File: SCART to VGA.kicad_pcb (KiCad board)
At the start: 2 copper layers, 44.4 x 63.5 mm, 14 parts, among them J1 SCART-F, J2 Conn_01x03_Male, J3 USB_B_Micro, J4 DB15_Female_HighDensity, J5 AudioJack3, U1 LM1881

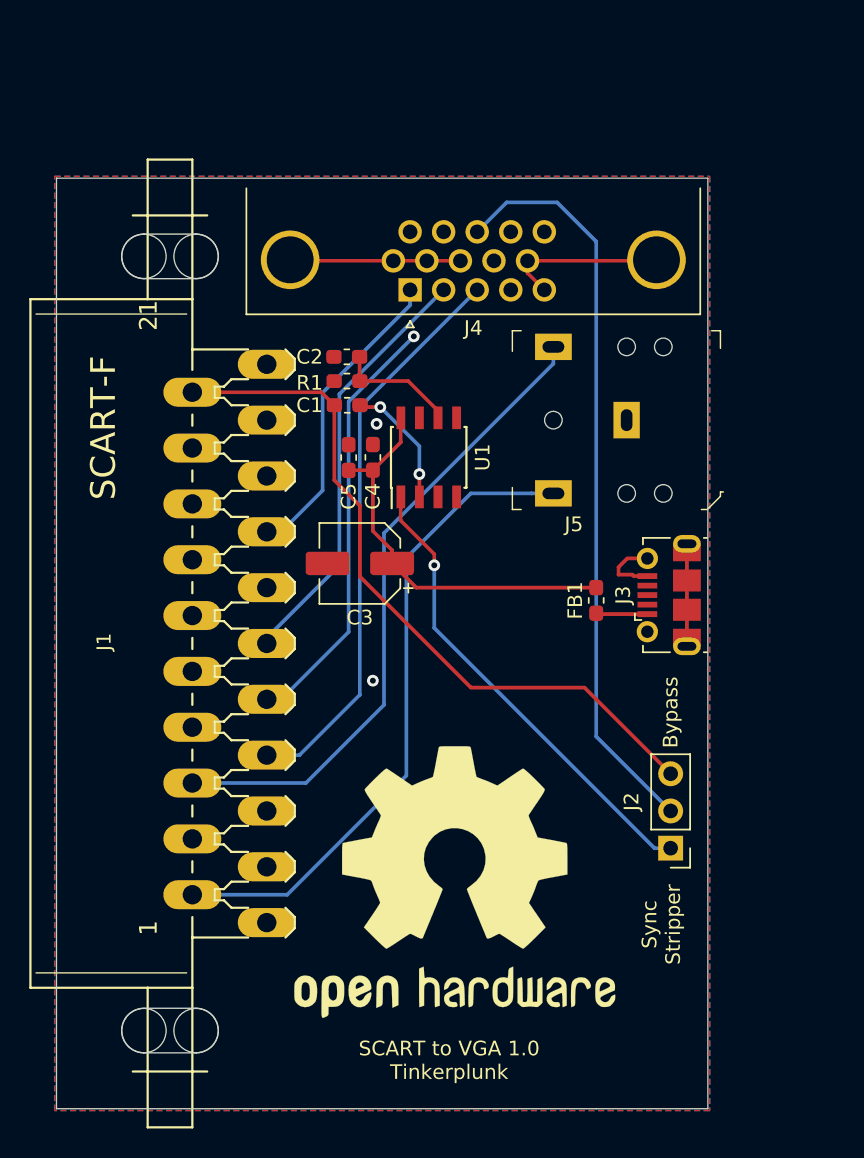
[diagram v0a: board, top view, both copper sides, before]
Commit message: Created branch
Branch where the SCART head lays on top of the PCB for direct plug in with a male hd-15 port.
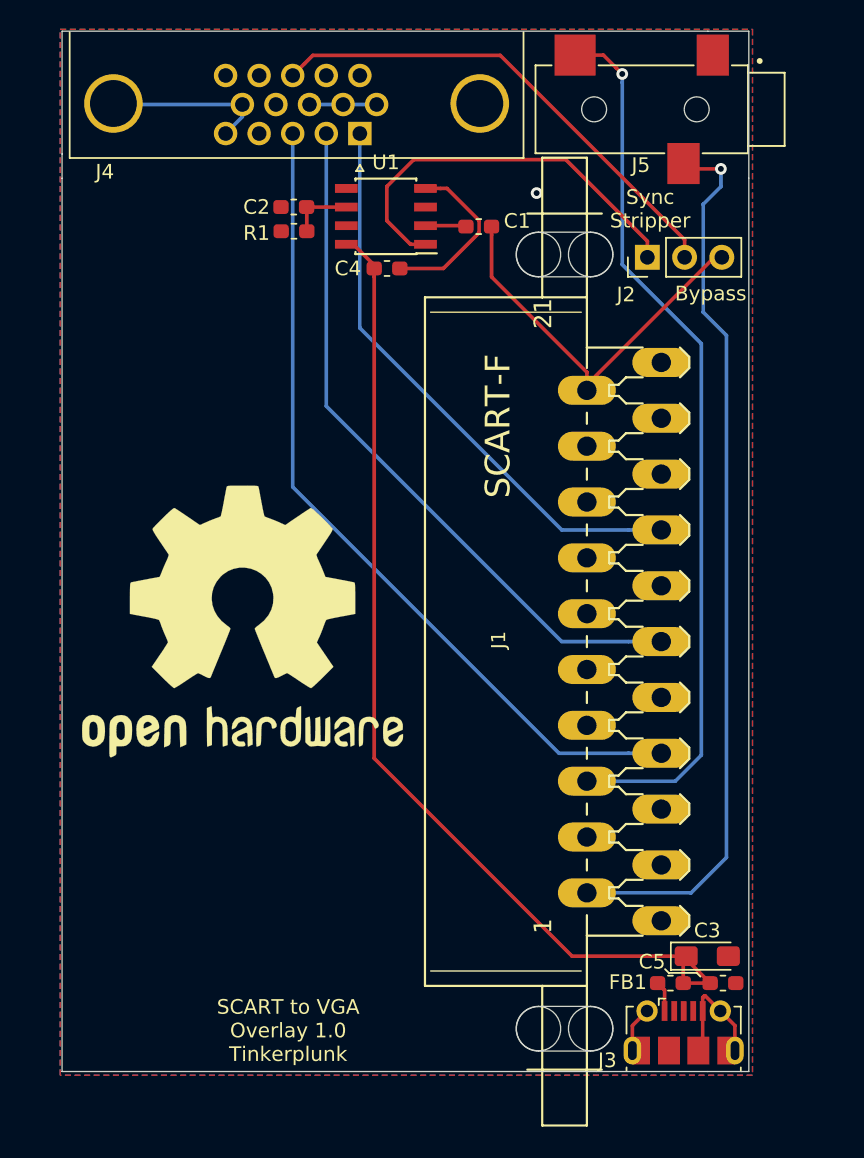
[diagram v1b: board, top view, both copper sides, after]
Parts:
- C3: footprint Capacitor_SMD:CP_Elec_5x5.3 -> Capacitor_Tantalum_SMD:CP_EIA-3216-18_Kemet-A_Pad1.58x1.35mm_HandSolder
- J4: footprint Connector_Dsub:DSUB-15-HD_Female_Horizontal_P2.29x1.98mm_EdgePinOffset3.03mm_Housed_MountingHolesOffset4.94mm -> Connector_Dsub:DSUB-15-HD_Male_Horizontal_P2.29x1.98mm_EdgePinOffset3.03mm_Housed_MountingHolesOffset4.94mm
- J5: footprint digikey-footprints:Headphone_Jack_3.5mm_SJ1-3523N -> SJ-3523-SMT-TR:CUI_SJ-3523-SMT-TR
- moved C5 44.0 mm to (120.4, 131.1), turned to 180 degrees
- moved J2 40.4 mm to (115.3, 81.6), turned to 90 degrees
- moved C3 35.8 mm to (119.3, 129.3), turned to 0 degrees
- moved J3 29.9 mm to (117.7, 134.5), turned to 0 degrees
- moved J1 26.9 mm to (111.1, 107.8)
- moved FB1 26.6 mm to (116.8, 131.1), turned to 0 degrees
- moved J5 23.4 mm to (118.6, 71.5)
- moved REF** 22.9 mm to (87.6, 106.4)
- moved U1 16.7 mm to (97.4, 78.8), turned to 180 degrees
- moved J4 16.6 mm to (91.1, 67.8)
- moved C1 15.1 mm to (103.7, 79.5), turned to 0 degrees
- moved C4 12.9 mm to (97.5, 82.4), turned to 180 degrees
- moved C2 10.8 mm to (91.1, 78.2)
- moved R1 10.8 mm to (91.1, 79.8)
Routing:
- net Net-(C3-Pad1): track 27.5 -> 69.3 mm
- net GND: track 63.6 -> 39.3 mm, vias 3 -> 1
- net SYNC_IN: track 49.2 -> 27.1 mm
- net GREEN: track 29.1 -> 48.1 mm
- net RED: track 21.1 -> 39.6 mm
- net BLUE: track 39.0 -> 56.8 mm
- net SYNC_OUT: track 51.0 -> 33.7 mm
- net RIGHT: track 44.7 -> 61.4 mm, vias 0 -> 1
- net LEFT: track 44.5 -> 61.0 mm, vias 0 -> 1
- net Net-(C1-Pad1): track 8.67 -> 2.79 mm, vias 2 -> 0
- net Net-(J2-Pad1): track 32.2 -> 27.6 mm, vias 1 -> 0
- net Net-(C2-Pad1): track 8.31 -> 4.37 mm
- net Net-(FB1-Pad1): track 3.51 -> 2.10 mm
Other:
- board size 44.4 x 63.5 mm -> 46.9 x 71 mm
- board text added: "SCART to VGA Overlay 1.0 Tinkerplunk"
- board text removed: "SCART to VGA 1.0 Tinkerplunk"

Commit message: 1.1 Update
Moved things around, made cutout for headphone jack, changed headphone jack part, added jumper for getting voltage optionally from the SCART socket.
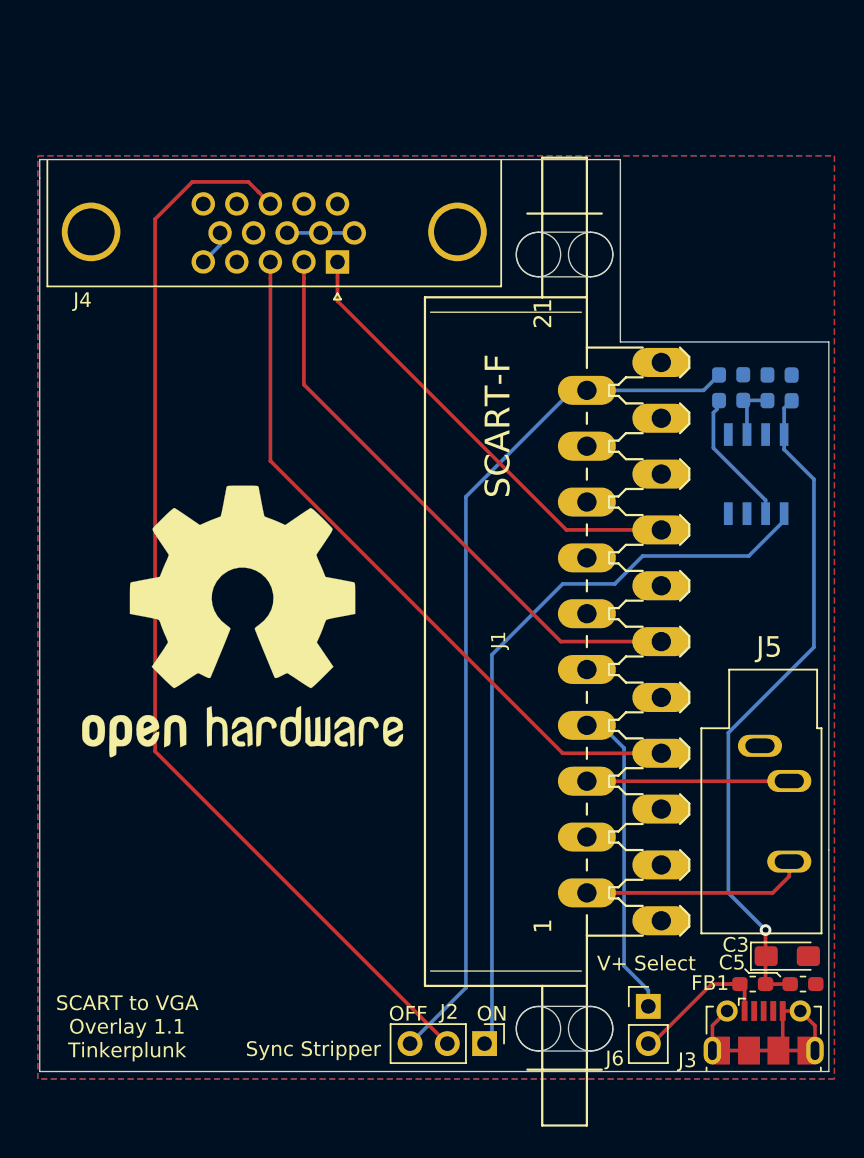
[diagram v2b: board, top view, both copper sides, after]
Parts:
- added J6: V+ Select, Connector_PinHeader_2.54mm:PinHeader_1x02_P2.54mm_Vertical, F.Cu at (115.3, 132.7)
- C1, C2, C4, R1, U1: moved to B.Cu
- J5: footprint SJ-3523-SMT-TR:CUI_SJ-3523-SMT-TR -> SJ1-3533NG:CUI_SJ1-3533NG
- moved J2 54.8 mm to (104.1, 135.3), turned to 270 degrees
- moved J5 43.6 mm to (122.9, 114.9), turned to 270 degrees
- moved R1 34.0 mm to (123.4, 90.5), turned to 90 degrees
- moved C2 33.1 mm to (121.8, 90.5), turned to 90 degrees
- moved U1 30.8 mm to (122.7, 96.4), turned to 90 degrees
- moved C4 28.8 mm to (125.1, 90.5), turned to 270 degrees
- moved C1 19.7 mm to (120.1, 90.5), turned to 90 degrees
- moved J4 8.89 mm to (89.5, 76.6)
- moved FB1 5.62 mm to (122.4, 131.2)
- moved C5 5.46 mm to (125.9, 131.2)
- moved C3 5.46 mm to (124.8, 129.3)
- moved J3 5.46 mm to (123.2, 134.5)
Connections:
- net Net-(FB1-Pad1) renamed SCART_VOLTAGE
- J4 pad 0: GND -> (no net)
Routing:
- net LEFT: track 61.0 -> 14.5 mm, vias 1 -> 0
- net RIGHT: track 61.4 -> 15.3 mm, vias 1 -> 0
- net SYNC_OUT: track 33.7 -> 74.1 mm
- net SYNC_IN: track 27.1 -> 59.6 mm
- net Net-(J2-Pad1): track 27.6 -> 51.0 mm
- net Net-(C3-Pad1): track 69.3 -> 46.0 mm, vias 0 -> 1
- net Net-(J1-Pad8): track 0.00 -> 21.5 mm
- net GND: track 39.3 -> 23.7 mm, vias 1 -> 0
- net RED: track 39.6 -> 31.2 mm
- net BLUE: track 56.8 -> 48.5 mm
- net GREEN: track 48.1 -> 40.0 mm
- net SCART_VOLTAGE: track 2.10 -> 9.91 mm
- net Net-(C1-Pad1): track 2.79 -> 8.85 mm
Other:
- board size 46.9 x 71 mm -> 53.8 x 62.2 mm
- board text added: "OFF"
- board text added: "ON"
- board text added: "SCART to VGA Overlay 1.1 Tinkerplunk"
- board text removed: "Bypass"
- board text removed: "SCART to VGA Overlay 1.0 Tinkerplunk"

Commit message: Direct Plug
Male VGA with vertical SCART connector for minimum horizontal footprint. Allows direct connection of SCART to VGA switchboxes such as Extron units, though only on the top row.
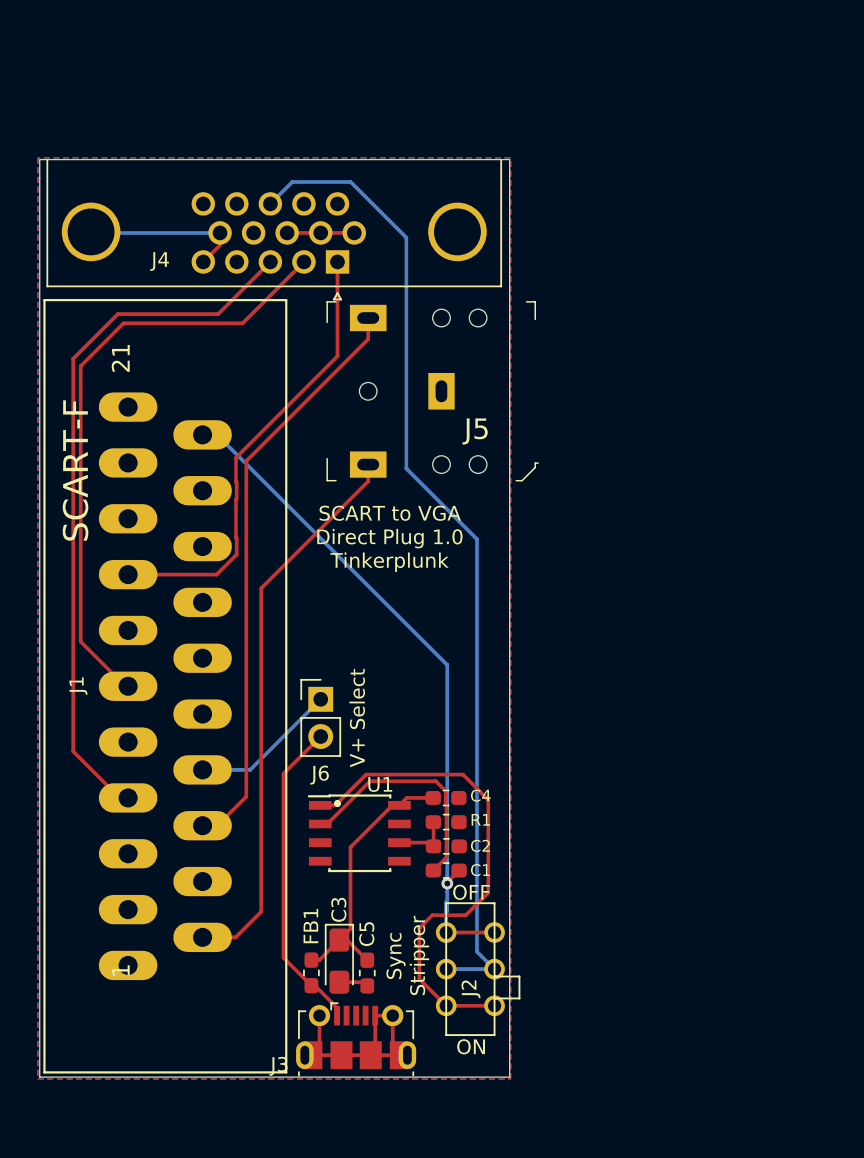
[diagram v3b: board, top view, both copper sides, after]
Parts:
- removed REF**: OSHW-Logo2_24.3x20mm_SilkScreen, Symbol:OSHW-Logo2_24.3x20mm_SilkScreen
- C1, C2, C4, R1, U1: moved to F.Cu
- J1: footprint SCART to DVI-A Compact:SCART-F -> SCART:SCART_F
- J2: footprint Connector_PinHeader_2.54mm:PinHeader_1x03_P2.54mm_Vertical -> SCART to DVI-A Compact:JS202011
- J5: footprint SJ1-3533NG:CUI_SJ1-3533NG -> digikey-footprints:Headphone_Jack_3.5mm_SJ1-3523N
- moved C1 37.8 mm to (101.5, 123.4), turned to 0 degrees
- moved C2 37.3 mm to (101.5, 121.8), turned to 0 degrees
- moved R1 36.9 mm to (101.5, 120.1), turned to 0 degrees
- moved C4 36.6 mm to (101.5, 118.5), turned to 180 degrees
- moved U1 36.5 mm to (95.6, 120.9), turned to 0 degrees
- moved J5 36.1 mm to (96.2, 90.7), turned to 180 degrees
- moved J6 30.6 mm to (93.0, 111.8)
- moved C3 30.6 mm to (94.2, 129.6), turned to 270 degrees
- moved FB1 30.1 mm to (92.3, 130.4), turned to 90 degrees
- moved C5 29.7 mm to (96.1, 130.4), turned to 90 degrees
- moved J1 28.9 mm to (82.4, 110.9)
- moved J3 27.8 mm to (95.4, 134.8)
- moved J2 5.18 mm to (103.1, 130.2), turned to 90 degrees
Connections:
- J4 pad 0: (no net) -> GND
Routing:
- net Net-(C3-Pad1): track 46.0 -> 18.6 mm, vias 1 -> 0
- net LEFT: track 14.5 -> 39.9 mm
- net RIGHT: track 15.3 -> 38.3 mm
- net Net-(J2-Pad1): track 51.0 -> 34.4 mm
- net SYNC_IN: track 59.6 -> 46.9 mm, vias 0 -> 1
- net SCART_VOLTAGE: track 9.91 -> 21.8 mm
- net Net-(J1-Pad8): track 21.5 -> 10.1 mm
- net GND: track 23.7 -> 34.6 mm
- net Net-(C1-Pad1): track 8.85 -> 15.9 mm
- net SYNC_OUT: track 74.1 -> 67.2 mm
- net GREEN: track 40.0 -> 41.5 mm
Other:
- board size 53.8 x 62.2 mm -> 32.1 x 62.6 mm
- board text added: "SCART to VGA Direct Plug 1.0 Tinkerplunk"
- board text removed: "SCART to VGA Overlay 1.1 Tinkerplunk"

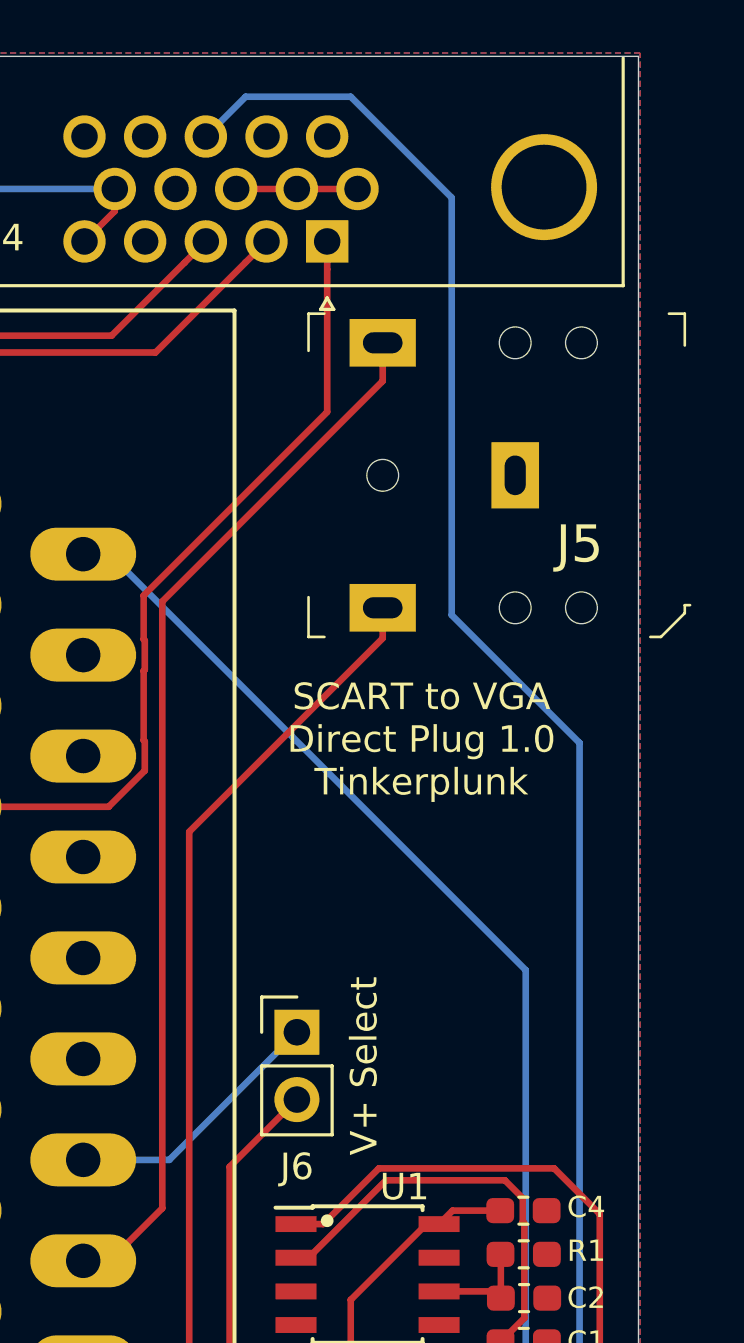
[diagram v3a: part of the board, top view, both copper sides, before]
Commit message: replaced and rotated headphone jack
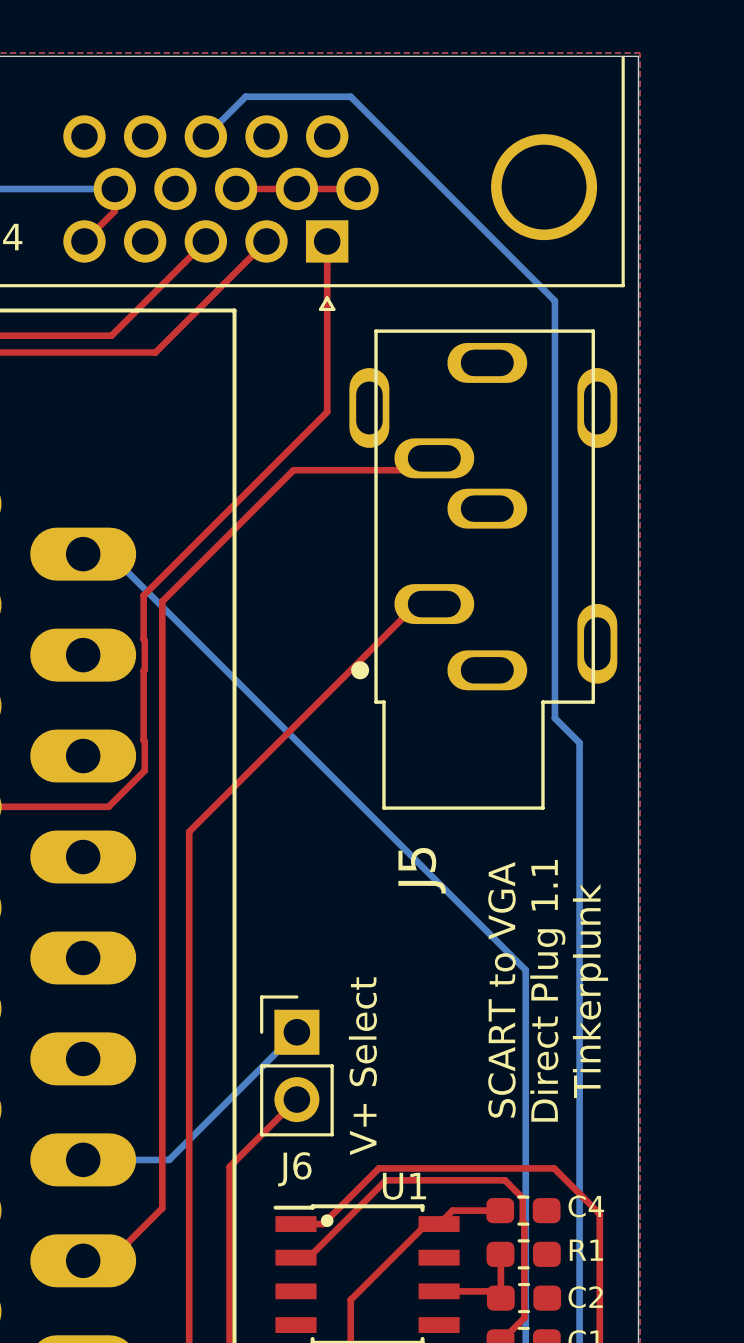
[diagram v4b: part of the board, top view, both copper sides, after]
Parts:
- J5: footprint digikey-footprints:Headphone_Jack_3.5mm_SJ1-3523N -> Tinkerplunk:CUI_SJ1-3533NG
- moved J5 8.35 mm to (100.2, 98.1), turned to 90 degrees
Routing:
- net RIGHT: track 38.3 -> 39.6 mm
- net LEFT: track 39.9 -> 39.2 mm
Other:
- board text added: "SCART to VGA Direct Plug 1.1 Tinkerplunk"
- board text removed: "SCART to VGA Direct Plug 1.0 Tinkerplunk"
